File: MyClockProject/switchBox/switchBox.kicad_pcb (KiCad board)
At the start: 2 copper layers, 114.3 x 81.3 mm, 19 parts, among them J1 RJ45, J6 Conn_01x16_Socket, J7 Conn_01x08_Socket, SW1 RotaryEncoder_Switch, SW2 S4_SW_Push, SW3 S3_SW_Push, SW4 S2_SW_Push, SW5 S1_SW_Push, SW6 MODE_SW_Push, U1 USB_C_Receptacle_PowerOnly_6P, U4 OLED_SSD1306_128x32_I2C

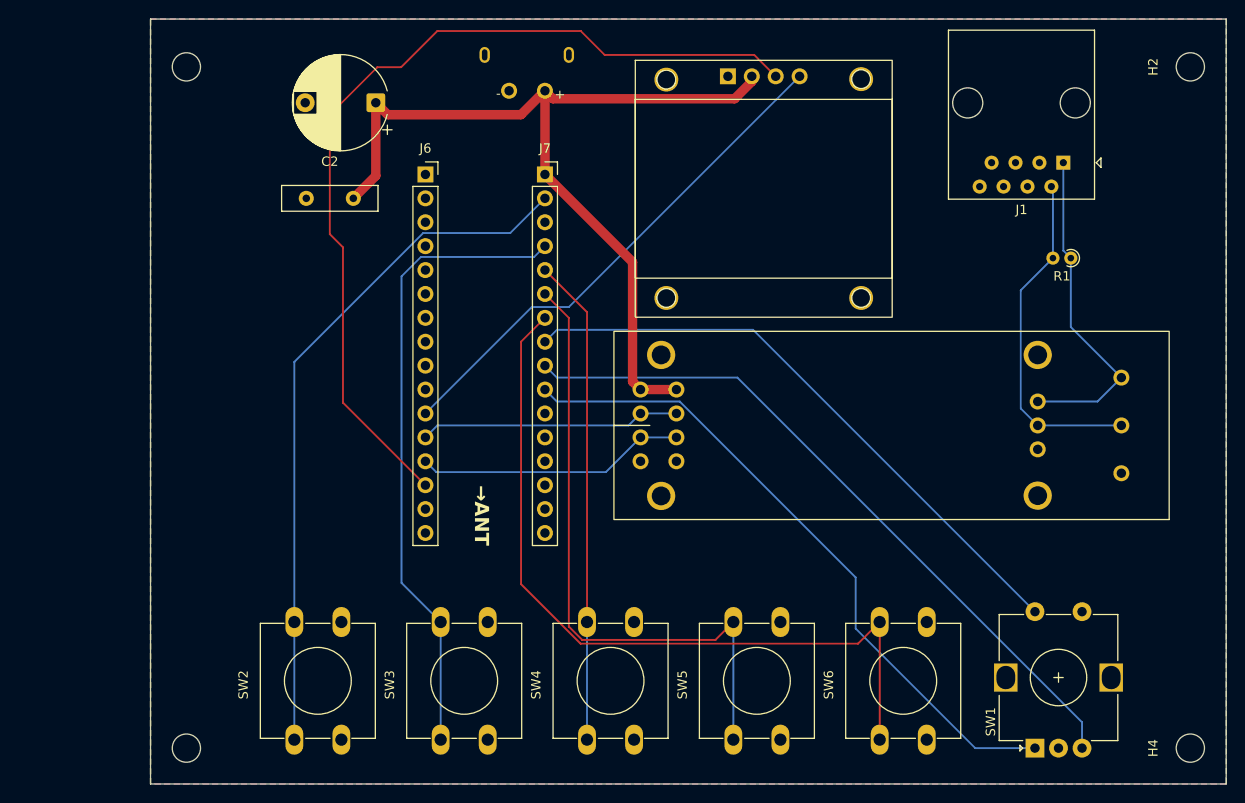
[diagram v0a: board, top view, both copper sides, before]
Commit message: コントロールボックスとモーター制御用の基盤設計を修正しました。（主にESP32ソケット幅変更）
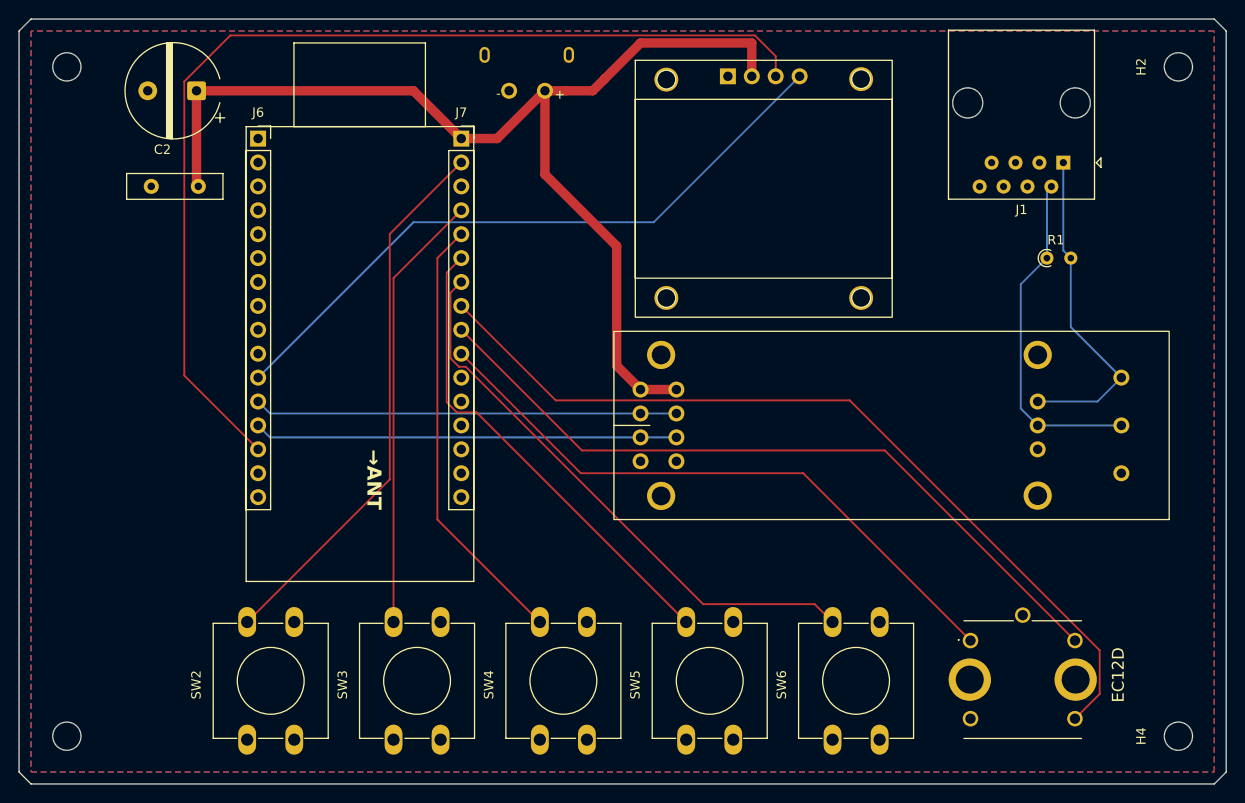
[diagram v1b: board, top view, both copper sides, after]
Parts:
- removed SW1: RotaryEncoder_Switch, Rotary_Encoder:RotaryEncoder_Alps_EC12E-Switch_Vertical_H20mm
- added RotaryEncoder: EC12D, clipboard:1481b7bd-967a-4c6f-926d-5fc3a8d29f51, F.Cu at (199.3, 152.4)
- moved J6 18.2 mm to (109.2, 87.6)
- moved C2 17.8 mm to (103.9, 82.5)
- moved C1 16.5 mm to (102.9, 92.7)
- moved H3 12.8 mm to (88.9, 151.1)
- moved H1 12.7 mm to (88.9, 80.0)
- moved J7 9.67 mm to (130.8, 87.6)
- moved SW6 5.01 mm to (170.3, 151.5)
- moved SW3 5.01 mm to (123.6, 151.5)
- moved SW2 5.01 mm to (108.1, 151.5)
- moved SW4 5.01 mm to (139.2, 151.5)
- moved SW5 5.01 mm to (154.7, 151.5)
- moved R1 2.54 mm to (193.0, 100.3), turned to 0 degrees
- moved H4 1.80 mm to (207.0, 151.1)
- moved H2 1.27 mm to (207.0, 80.0)
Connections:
- R1 pad 1: Net-(J1-Pin_1) -> Net-(J1-Pin_2)
- R1 pad 2: Net-(J1-Pin_2) -> Net-(J1-Pin_1)
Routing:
- net /Net-(J7_Pin_25): track 65.0 -> 91.3 mm
- net Net-(U1-VDD): track 94.1 -> 118.9 mm
- net /Net-(J7-Pin_26): track 83.5 -> 60.8 mm
- net /Net-(J7-Pin_12): track 67.5 -> 46.7 mm
- net Net-(J6-Pin_RXI): track 27.7 -> 45.0 mm
- net /Net-(J7-Pin_27): track 67.8 -> 51.1 mm
- net Net-(J6-Pin_TXO): track 28.7 -> 45.0 mm
- net Net-(J6-Pin_21): track 54.6 -> 70.8 mm
- net /Net-(J7-Pin_13): track 74.0 -> 58.3 mm
- net Net-(J6-Pin_22): track 96.6 -> 110.3 mm
- net /Net-(J7-Pin_14): track 51.8 -> 46.8 mm
- net /Net-(J7-Pin_32): track 71.0 -> 66.7 mm
- net /Net-(J7-Pin_33): track 75.5 -> 78.9 mm
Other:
- board size 114.3 x 81.3 mm -> 128.3 x 81.3 mm
